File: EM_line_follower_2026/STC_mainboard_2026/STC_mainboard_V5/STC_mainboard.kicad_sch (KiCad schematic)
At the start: 108 parts, among them J1 Conn_01x04, J10 Conn_01x04, J11 WirePad, J12 WirePad, J15 WirePad, J16 WirePad, J2 WirePad, J20 WirePad, J21 WirePad, J3 WirePad, J4 Conn_01x02, J5 WirePad, J6 WirePad, J7 WirePad, J8 WirePad, J9 WirePad, P1 ${VALUE}, P2 ${VALUE}, SW1 SW_Push, SW3 SW_Push, U1 STC16H40K128_CoreBoard, U11 TPS54360DDA, U3 LSM6DSRTR, U4 LM1117-3.3V, U5 OPA2197xD, U6 OPA2197xD, U7 OPA2197xD

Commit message: upload intern pcb
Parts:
- removed R3: 0R, HKUST_RDC2025_Footprint_Lib:R_0603_1608Metric, symbol HKUST_RDC2024_Symbol_Lib:R_Small_US
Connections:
- net +5V: now also C10.1, C9.1, L1.2, R1.2
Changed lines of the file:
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@@
 	(wire
 		(pts
-			(xy 283.21 340.36) (xy 288.29 340.36)
-		)
-		(stroke
-			(width 0)
-			(type default)
-		)
-	)
-	(wire
-		(pts
 			(xy 419.1 31.75) (xy 419.1 40.64)
 		)
@@
 	(wire
 		(pts
-			(xy 264.16 340.36) (xy 278.13 340.36)
+			(xy 264.16 340.36) (xy 288.29 340.36)
 		)
 		(stroke
@@
 					(unit 1)
 				)
-			)
-		)
-	)
-	(symbol
-		(lib_id "HKUST_RDC2024_Symbol_Lib:R_Small_US")
-		(at 280.67 340.36 270)
-		(unit 1)
-		(exclude_from_sim no)
-		(in_bom yes)
-		(on_board yes)
-		(dnp no)
-		(property "Reference" "R3"
-			(at 280.67 334.01 90)
-			(effects
-				(font
-					(size 1.27 1.27)
-				)
-			)
-		)
-		(property "Value" "0R"
-			(at 280.67 336.55 90)
-			(effects
-				(font
-					(size 1.27 1.27)
-				)
-			)
-		)
-		(property "Footprint" "HKUST_RDC2025_Footprint_Lib:R_0603_1608Metric"
-			(at 280.67 340.36 0)
-			(effects
-				(font
-					(size 1.27 1.27)
-				)
-				(hide yes)
-			)
-		)
-		(property "Datasheet" ""
-			(at 280.67 340.36 0)
-			(effects
-				(font
-					(size 1.27 1.27)
-				)
-				(hide yes)
-			)
-		)
-		(property "Description" ""
-			(at 280.67 340.36 0)
-			(effects
-				(font
-					(size 1.27 1.27)
-				)
-				(hide yes)
-			)
-		)
-		(pin "1"
-		)
-		(pin "2"
-		)
-		(instances
-			(project "STC_mainboard"
-				(path "/3dbd0099-64a2-40b8-9866-2cb85c958c5c"
-					(reference "R3")
-					(unit 1)
-				)

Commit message: modify STM mainboard V5
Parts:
- removed C10: 10V 1000uF, HKUST_RDC2025_Footprint_Lib:CP_Radial_D8.0mm_P12.00mm, symbol HKUST_RDC2024_Symbol_Lib:CP1_Small
- removed C29: 47uF, HKUST_RDC2024_Footprint_Lib:C_0603_1608Metric, symbol HKUST_RDC2024_Symbol_Lib:C_Small
- removed C5, C6: 2.2uF, HKUST_RDC2025_Footprint_Lib:C_0603_1608Metric, symbol HKUST_RDC2024_Symbol_Lib:C_Small
- removed C7: 39pF, HKUST_RDC2025_Footprint_Lib:C_0603_1608Metric, symbol HKUST_RDC2024_Symbol_Lib:C_Small
- removed C8: 100nF, HKUST_RDC2025_Footprint_Lib:C_0603_1608Metric, symbol HKUST_RDC2024_Symbol_Lib:C_Small
- removed C9: 10uF, HKUST_RDC2025_Footprint_Lib:C_0603_1608Metric, symbol HKUST_RDC2024_Symbol_Lib:C_Small
- removed D17: MM3Zxx, Diode_SMD:D_SOD-323F, symbol Diode:MM3Zxx
- removed D2: SS54, HKUST_RDC2025_Footprint_Lib:D_SMA, symbol HKUST_RDC2024_Symbol_Lib:SS54
- removed J15, J16: WirePad, China5.0:WirePad_motor, symbol Connector:Conn_01x01_Pin
- removed J4: Conn_01x02, Connector_JST:JST_XH_B2B-XH-A_1x02_P2.50mm_Vertical, symbol STC:Conn_01x02
- removed L1: 22uH, HKUST_RDC2025_Footprint_Lib:L_7.3x7.3_H3.5, symbol HKUST_RDC2024_Symbol_Lib:L_Small
- removed R1: 53.6k, HKUST_RDC2025_Footprint_Lib:R_0603_1608Metric, symbol HKUST_RDC2024_Symbol_Lib:R_Small_US
- removed R2: 10.2k, HKUST_RDC2025_Footprint_Lib:R_0603_1608Metric, symbol HKUST_RDC2024_Symbol_Lib:R_Small_US
- removed R4: 162k, HKUST_RDC2025_Footprint_Lib:R_0603_1608Metric, symbol HKUST_RDC2024_Symbol_Lib:R_Small_US
- removed R53: 1k, HKUST_RDC2024_Footprint_Lib:R_0603_1608Metric, symbol HKUST_RDC2024_Symbol_Lib:R_Small_US
- removed U10: ~, Package_SO:SOIC-8-1EP_3.9x4.9mm_P1.27mm_EP2.29x3mm, symbol AT8236:AT8236
- removed U11: TPS54360DDA, HKUST_RDC2025_Footprint_Lib:SOIC-8_3.9x4.9mm_P1.27mm, symbol HKUST_RDC2024_Symbol_Lib:TPS54360DDA
- added 1, 11, 111: ~, ProLib_1pcs_2026-06-16.elibz:BT2.0, symbol ProLib_1pcs_2026-06-16.elibz:BT2.0
- added C10: 1000uF, Capacitor_SMD:CP_Elec_4x5.3, symbol STC:CP1_Small
- added C2: 47uF, HKUST_RDC2024_Footprint_Lib:C_0603_1608Metric, symbol HKUST_RDC2024_Symbol_Lib:C_Small
- added C5, C6: 2.2uF, HKUST_RDC2024_Footprint_Lib:C_0603_1608Metric, symbol STC:C_Small
- added C7: 100nF, HKUST_RDC2024_Footprint_Lib:C_0603_1608Metric, symbol STC:C_Small
- added C8: 39F, HKUST_RDC2024_Footprint_Lib:C_0603_1608Metric, symbol STC:C_Small
- added C9: 10uF, HKUST_RDC2024_Footprint_Lib:C_0603_1608Metric, symbol STC:C_Small
- added D1: SS54, HKUST_RDC2024_Footprint_Lib:D_SMA, symbol STC:D_Schottky
- added D2: MM3Zxx, Diode_SMD:D_SOD-323F, symbol Diode:MM3Zxx
- added J23, J24: WirePad, China5.0:WirePad_motor, symbol Connector:Conn_01x01_Pin
- added L1: 22uH, HKUST_RDC2024_Footprint_Lib:L_7.3x7.3_H3.5, symbol STC:L_Small
- added R1: 162k, HKUST_RDC2024_Footprint_Lib:R_0603_1608Metric, symbol STC:R_Small_US
- added R2: 53.6k, HKUST_RDC2024_Footprint_Lib:R_0603_1608Metric, symbol STC:R_Small_US
- added R3: 10.2k, HKUST_RDC2024_Footprint_Lib:R_0603_1608Metric, symbol STC:R_Small_US
- added R4: 0R, HKUST_RDC2024_Footprint_Lib:R_0603_1608Metric, symbol STC:R_Small_US
- added R5: 1k, HKUST_RDC2024_Footprint_Lib:R_0603_1608Metric, symbol HKUST_RDC2024_Symbol_Lib:R_Small_US
- added U10: TPS54360DDA, Package_SO:TI_SO-PowerPAD-8_ThermalVias, symbol STC:TPS54360DDA
- added U2: ~, Package_SO:SOIC-8-1EP_3.9x4.9mm_P1.27mm_EP2.29x3mm, symbol AT8236:AT8236
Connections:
- net +12V: now also 111.2 (+), C2.1, C5.1, C6.1, R5.2, U10.2 (VIN), U2.5 (VM)
- net +5V: now also R4.2
- net FB: now also R2.2, R3.1, U10.5 (FB)
- net GND: now also 1.1 (-), C10.2, C2.2, C5.2, C6.2, C8.2, C9.2, D1.2 (A), D2.2 (A), R1.2, R3.2, U10.7 (GND), U10.9 (GNDPAD), U2.1 (GND), U2.7 (ISEN), U2.9 (EP)
- net P6.0: now also U8.2 (IN2); no longer U8.3 (IN1)
- net P6.2: now also U8.3 (IN1); no longer U8.2 (IN2)
- net P6.4: now also U9.2 (IN2); no longer U9.3 (IN1)
- net P6.6: now also U9.3 (IN1); no longer U9.2 (IN2)
- net P7.4: now also U2.2 (IN2)
- net P7.6: now also U2.3 (IN1)
- net fan1: now also J24.1 (Pin_1), U2.6 (OUT1)
- net fan2: now also J23.1 (Pin_1), U2.8 (OUT2)
- new net: D2.1 (K), R5.1, U2.4 (VREF)
- new net: R1.1, U10.4 (RT/CLK)
- new net: C7.2, D1.1 (K), L1.1, U10.8 (SW)
- new net: C7.1, U10.1 (BOOT)
- new net: C8.1, U10.6 (COMP)
- new net: C10.1, C9.1, L1.2, R2.1, R4.1
- new net: 11.2 (+), 111.1 (-)
- new net: 1.2 (+), 11.1 (-)
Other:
- note removed: "12V to 5V"

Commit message: first draft for V5 need to redraw the buzzer footprint and reduce the length of the board
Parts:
- removed J12, J9: WirePad, China5.0:WirePad_motor, symbol Connector:Conn_01x01_Pin
- removed R4: 0R, HKUST_RDC2024_Footprint_Lib:R_0603_1608Metric, symbol STC:R_Small_US
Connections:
- net +5V: now also C10.1, C9.1, L1.2, R2.1

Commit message: finish the V5 design
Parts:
- removed P1, P2: ${VALUE}, 2K0300久久派_主板_V1.0:ECD-GH1.25-6P-SH, symbol STC8H&16F&32G_主板_V2.3:Header-D-M 2x3P
- added J12, J14, J15, J16: WirePad, STC_mainboard_lib:WirePad_motor, symbol Connector:Conn_01x01_Pin
- added J13: Conn_01x02, Connector_AMASS:AMASS_XT30U-M_1x02_P5.0mm_Vertical, symbol Connector_Generic:Conn_01x02
- added J4, J9: Conn_01x04, Connector_JST:JST_GH_BM04B-GHS-TBT_1x04-1MP_P1.25mm_Vertical, symbol STC:Conn_01x04
- B1: footprint 龙芯LS2K0300主板V2.0:BEEP 9x5.5mm -> Inductor_SMD:L_12x12mm_H4.5mm
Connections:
- net +12V: now also J13.2 (Pin_2)
- net +3.3V: now also J12.1 (Pin_1), J14.1 (Pin_1)
- net +5V: now also J15.1 (Pin_1), J16.1 (Pin_1), J4.2 (Pin_2), J9.2 (Pin_2)
- net GND: now also J13.1 (Pin_1), J4.1 (Pin_1), J9.1 (Pin_1)
- net P3.4: now also J9.3 (Pin_3)
- net P3.5: now also J4.3 (Pin_3)
- net P5.0: now also J9.4 (Pin_4)
- net P5.1: now also J4.4 (Pin_4)
- net P7.4: now also U2.3 (IN1); no longer U2.2 (IN2)
- net P7.6: now also U2.2 (IN2); no longer U2.3 (IN1)
- no-connect marks 56 -> 52

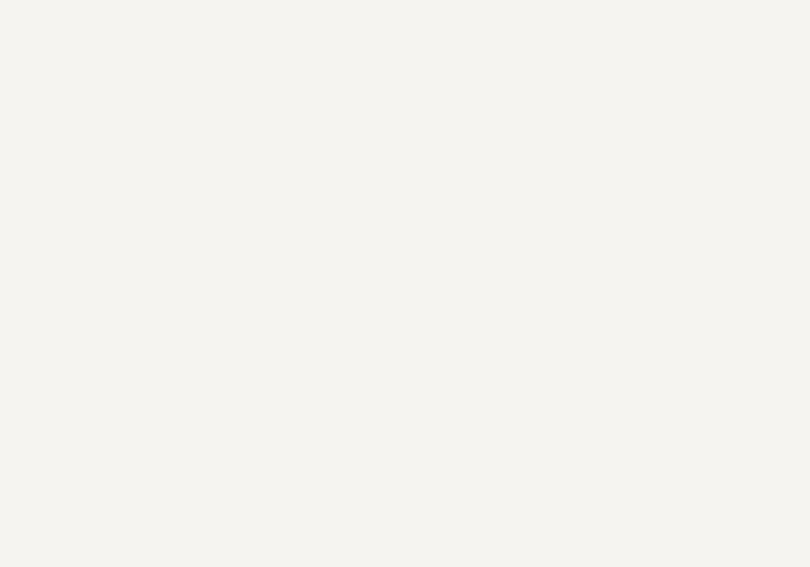
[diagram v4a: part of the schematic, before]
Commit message: change position of variable resistor
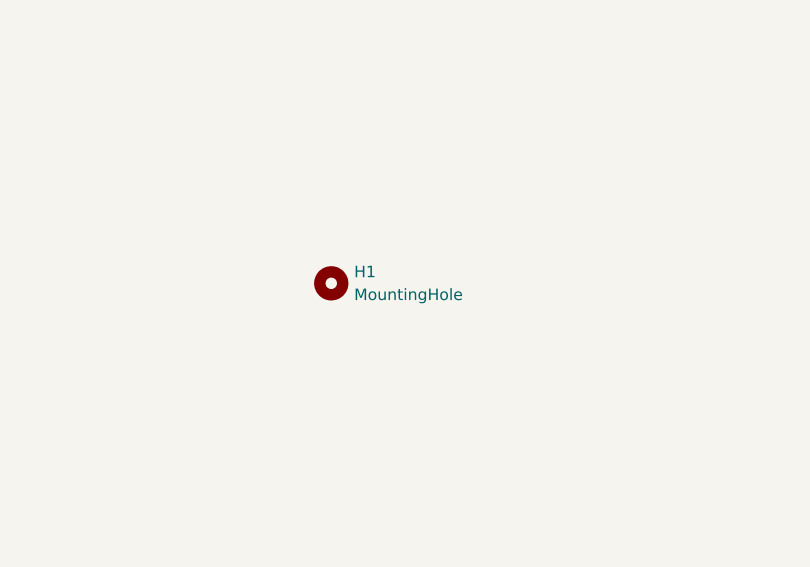
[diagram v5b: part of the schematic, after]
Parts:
- added H1: MountingHole, MountingHole:MountingHole_2.2mm_M2, symbol China5.0:MountingHole
- 1, 11, 111, U2, U8, U9: value ~ -> (none)
